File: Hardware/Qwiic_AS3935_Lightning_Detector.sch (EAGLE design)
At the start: 28 parts, among them U1 AS3935

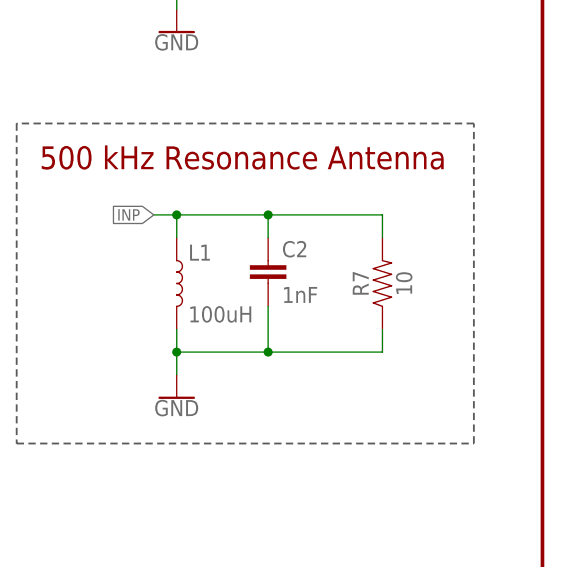
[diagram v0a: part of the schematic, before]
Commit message: Fixed AS3935 SKU in library
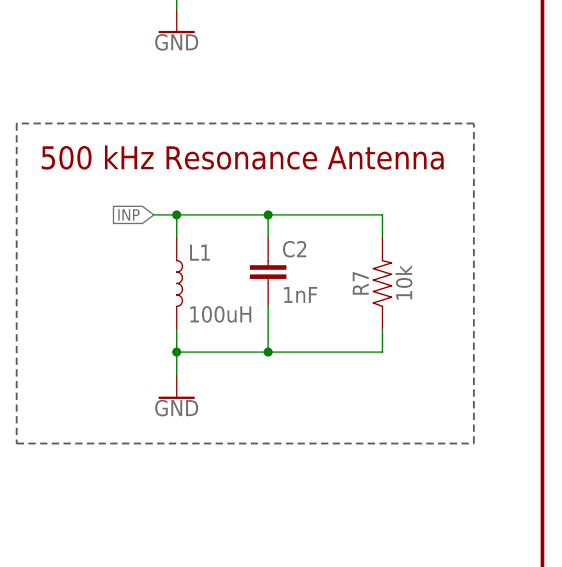
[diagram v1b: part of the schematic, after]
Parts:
- R7: value 10 -> 10k; device SparkFun-Resistors:10OHM-0603-1/10W-1% -> SparkFun-Resistors:10KOHM-0603-1/10W-1%
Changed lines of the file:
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@@
 <part name="C3" library="SparkFun-Capacitors" deviceset="10UF" device="-0603-6.3V-20%" value="10uF"/>
 <part name="GND10" library="SparkFun-PowerSymbols" deviceset="GND" device=""/>
-<part name="R7" library="SparkFun-Resistors" deviceset="10OHM" device="-0603-1/10W-1%" value="10"/>
+<part name="R7" library="SparkFun-Resistors" deviceset="10KOHM" device="-0603-1/10W-1%" value="10k"/>
 <part name="JP4" library="SparkFun-Jumpers" deviceset="JUMPER-SMT_3_2-NC_TRACE" device="_SILK"/>
 <part name="H1" library="SparkFun-Hardware" deviceset="STAND-OFF" device="TIGHT"/>

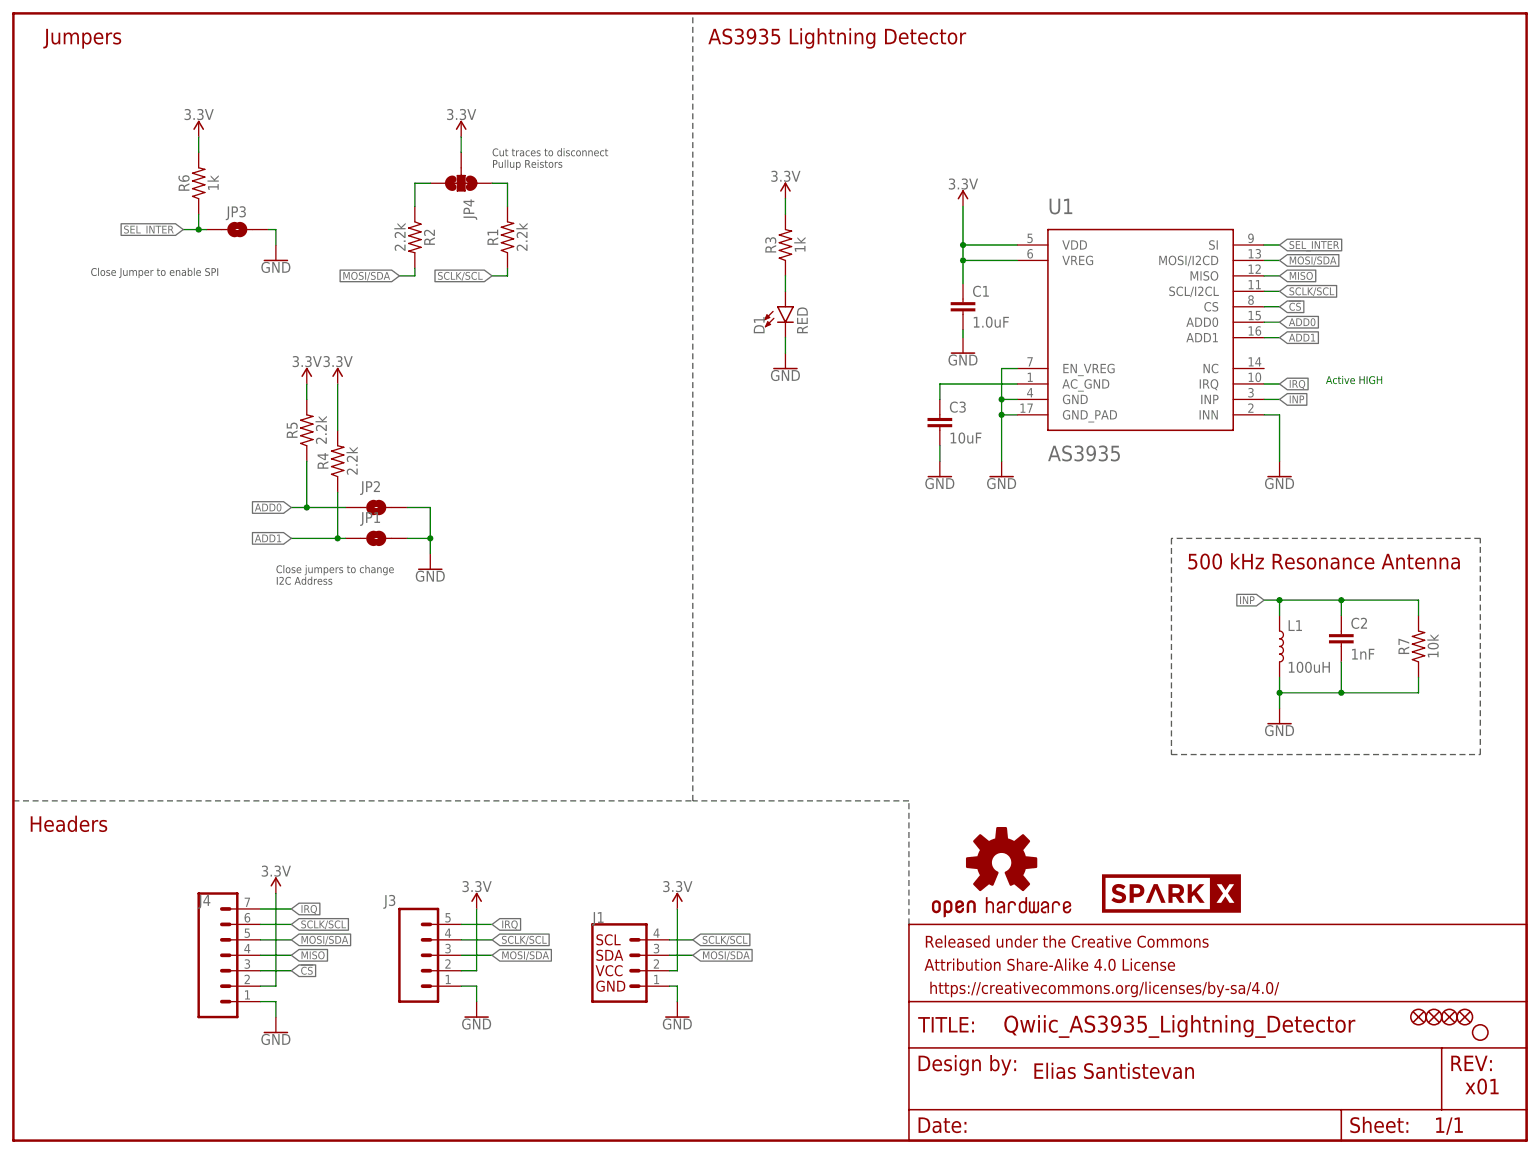
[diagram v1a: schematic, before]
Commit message: Version x02 Exposed pad underneath was not connected to ground, coil package was incorrect.
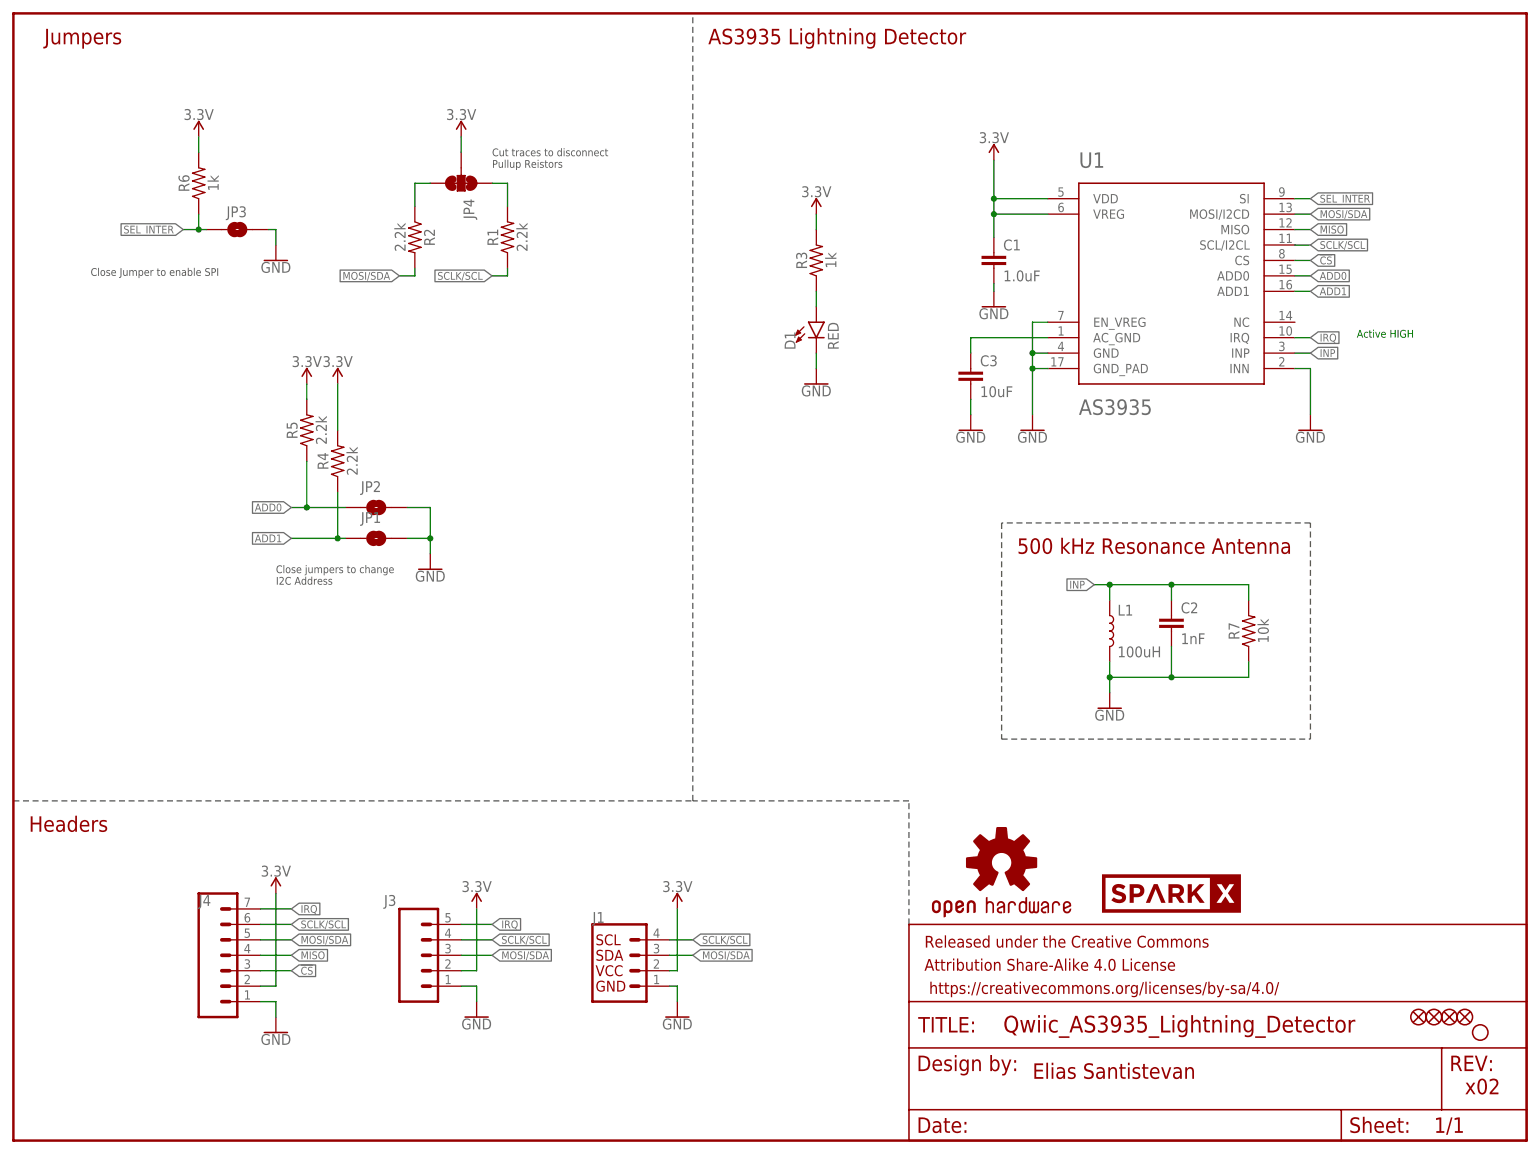
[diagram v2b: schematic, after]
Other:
- note added: "x02"
- note removed: "x01"
- moved on the sheet: C1, C2, C3, D1, L1, R3, R7, U1

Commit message: Updates README and deletes unnecssary production files.
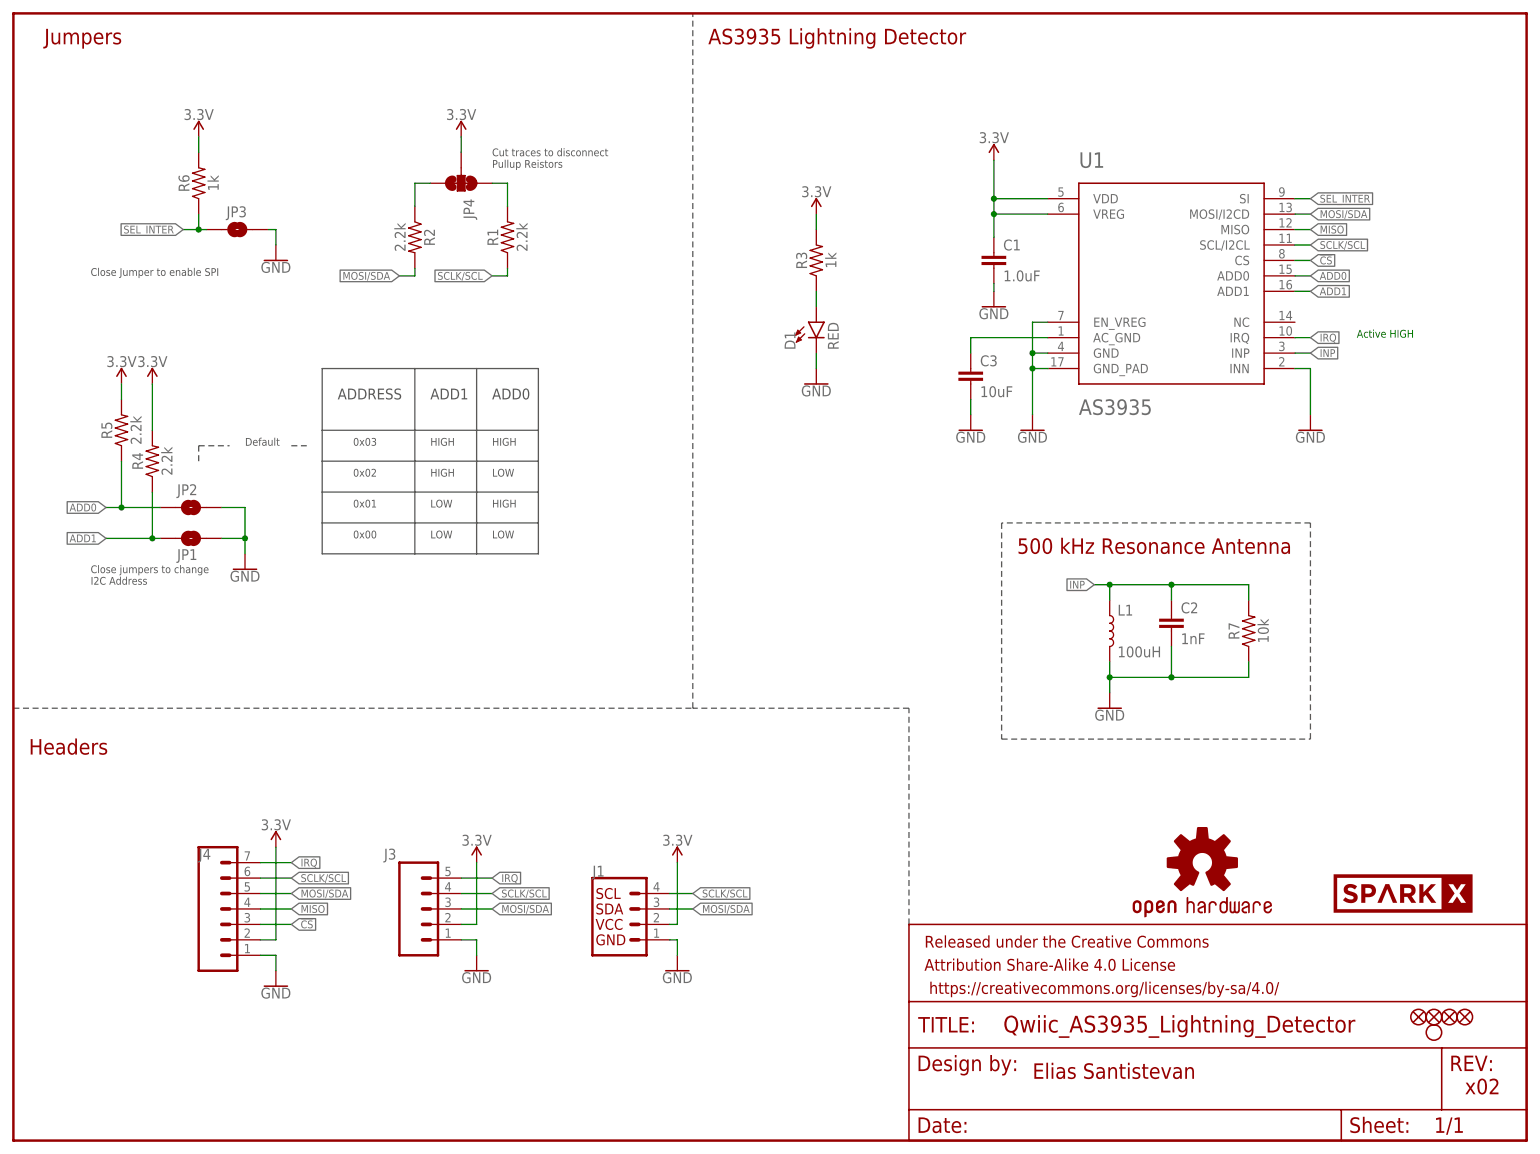
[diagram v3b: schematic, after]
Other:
- note added: "0x00"
- note added: "0x01"
- note added: "0x02"
- note added: "0x03"
- note added: "ADD0"
- note added: "ADD1"
- note added: "ADDRESS"
- note added: "Default"
- note added: "HIGH"
- note added: "LOW"
- moved on the sheet: J1, J3, J4, JP1, JP2, R4, R5
